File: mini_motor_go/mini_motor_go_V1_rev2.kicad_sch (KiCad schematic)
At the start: 30 parts, among them J10 Conn_01x02_Pin, J11 USB4520-03-0-A_REVA, J12 BM05B-SRSS-TB_LF__SN_, J13 BM05B-SRSS-TB_LF__SN_, J3 I2C_STANDARDQWIIC, J5 I2C_STANDARDQWIIC, J9 Conn_01x09_Pin, U1 ESP32-S3-WROOM-1

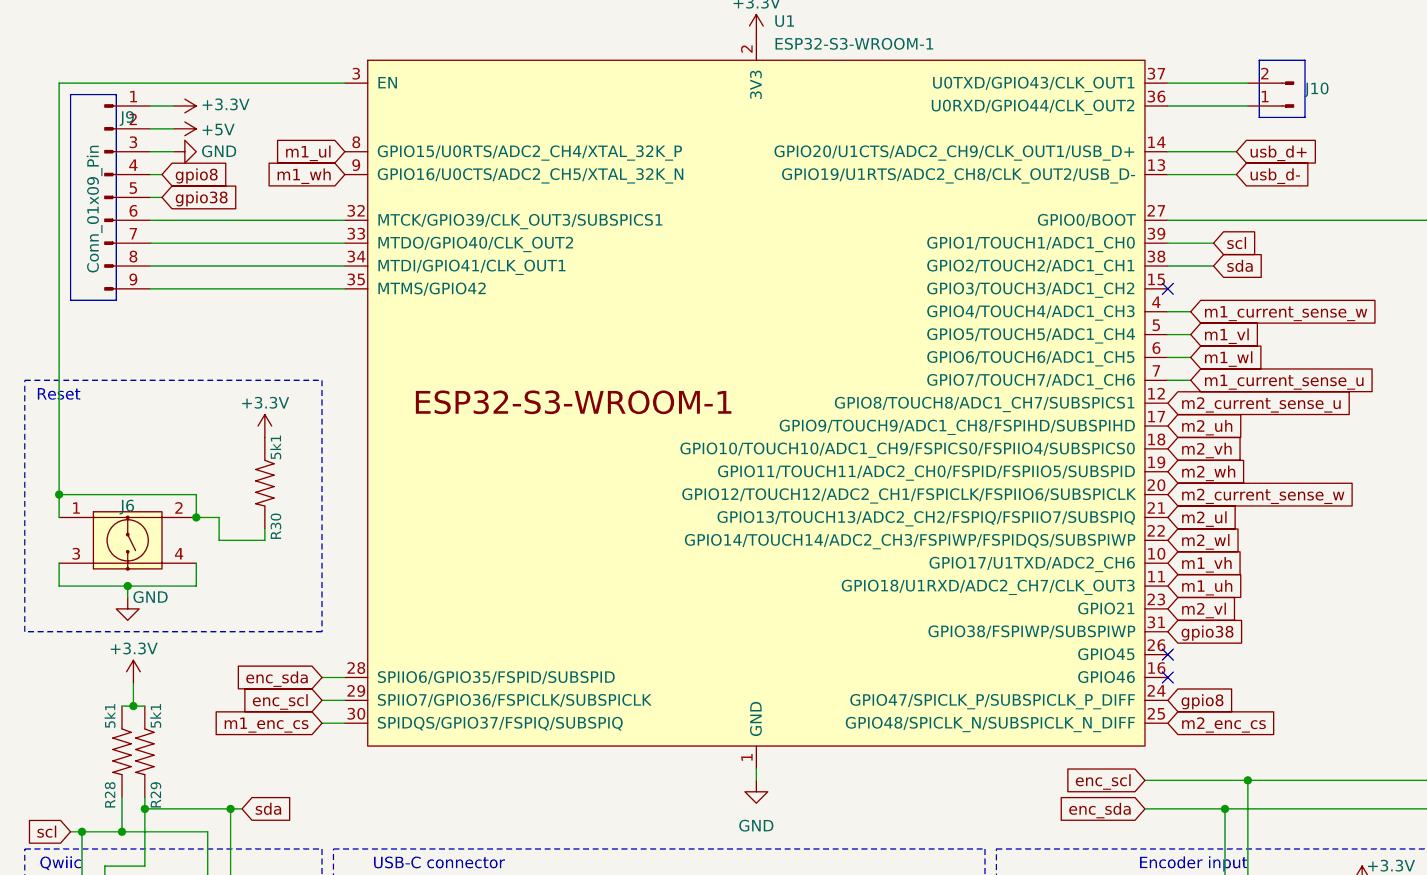
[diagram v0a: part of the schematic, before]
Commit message: slight update to part selection table
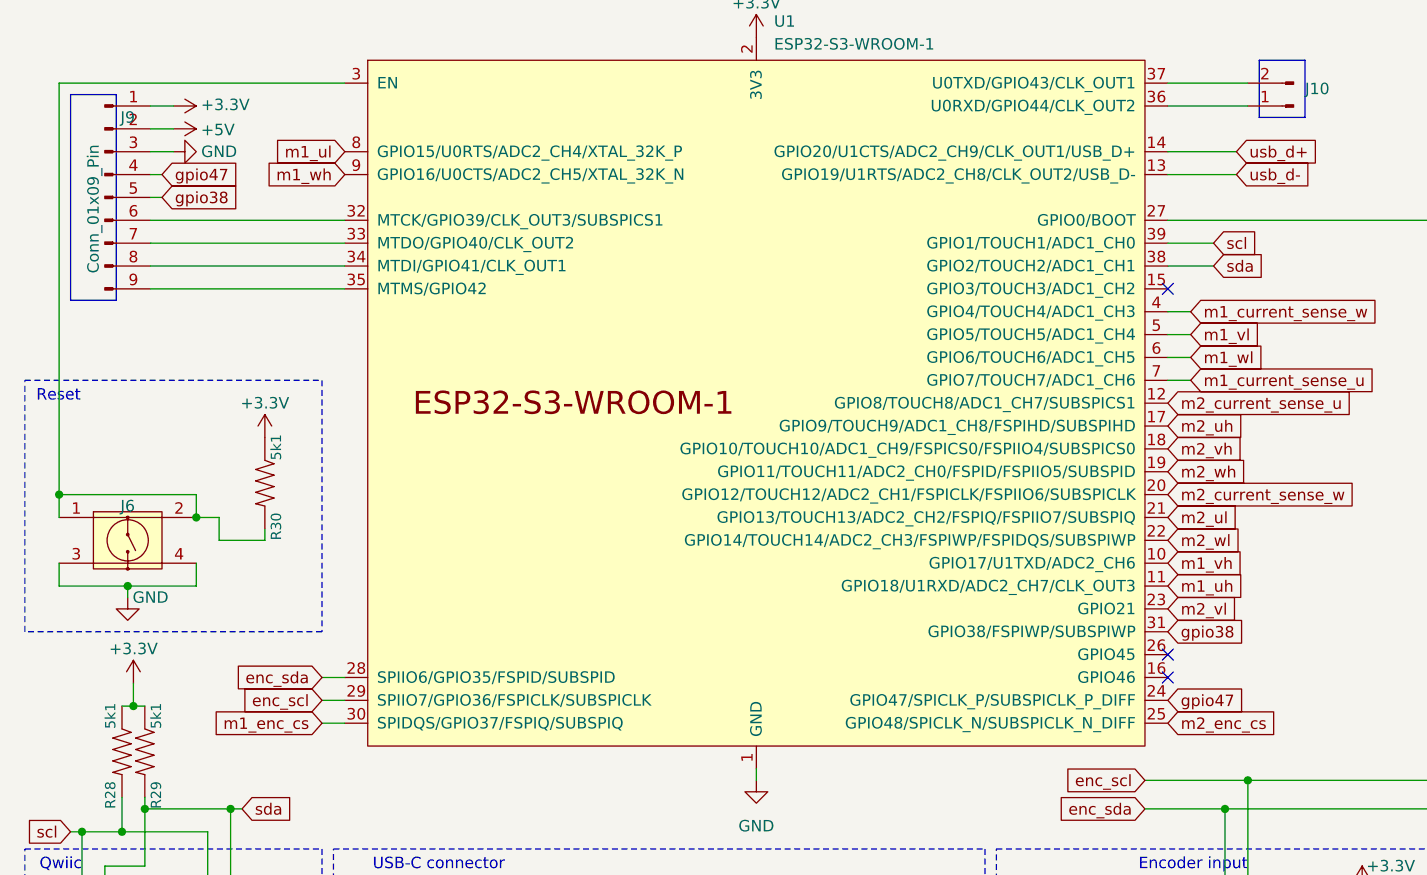
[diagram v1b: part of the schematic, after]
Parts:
- D1, D2, D3: footprint LED_SMD:LED_0805_2012Metric_Pad1.15x1.40mm_HandSolder -> LED_SMD:LED_0805_2012Metric
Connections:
- net gpio8: no longer J9.4 (Pin_4), U1.24 (GPIO47/SPICLK_P/SUBSPICLK_P_DIFF)
- new net gpio47: J9.4 (Pin_4), U1.24 (GPIO47/SPICLK_P/SUBSPICLK_P_DIFF)
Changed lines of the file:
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@@
     )
   )
-  (global_label "gpio8" (shape input) (at 29.21 40.64 0) (fields_autoplaced)
-    (effects (font (size 1.27 1.27)) (justify left))
-    (property "Intersheetrefs" "${INTERSHEET_REFS}" (at 37.3771 40.64 0)
+  (global_label "gpio47" (shape input) (at 29.21 40.64 0) (fields_autoplaced)
+    (effects (font (size 1.27 1.27)) (justify left))
+    (property "Intersheetrefs" "${INTERSHEET_REFS}" (at 38.5866 40.64 0)
       (effects (font (size 1.27 1.27)) (justify left) hide)
     )
@@
     )
   )
-  (global_label "gpio8" (shape input) (at 140.97 99.06 0) (fields_autoplaced)
-    (effects (font (size 1.27 1.27)) (justify left))
-    (property "Intersheetrefs" "${INTERSHEET_REFS}" (at 149.1371 99.06 0)
+  (global_label "gpio47" (shape input) (at 140.97 99.06 0) (fields_autoplaced)
+    (effects (font (size 1.27 1.27)) (justify left))
+    (property "Intersheetrefs" "${INTERSHEET_REFS}" (at 150.3466 99.06 0)
       (effects (font (size 1.27 1.27)) (justify left) hide)
     )
@@
       (effects (font (size 1.27 1.27)) (justify right))
     )
-    (property "Footprint" "LED_SMD:LED_0805_2012Metric_Pad1.15x1.40mm_HandSolder" (at 38.1 176.53 0)
+    (property "Footprint" "LED_SMD:LED_0805_2012Metric" (at 38.1 176.53 0)
       (effects (font (size 1.27 1.27)) hide)
     )
@@
       (effects (font (size 1.27 1.27)) (justify right))
     )
-    (property "Footprint" "LED_SMD:LED_0805_2012Metric_Pad1.15x1.40mm_HandSolder" (at 19.05 176.53 0)
+    (property "Footprint" "LED_SMD:LED_0805_2012Metric" (at 19.05 176.53 0)
       (effects (font (size 1.27 1.27)) hide)
     )
@@
       (effects (font (size 1.27 1.27)) (justify right))
     )
-    (property "Footprint" "LED_SMD:LED_0805_2012Metric_Pad1.15x1.40mm_HandSolder" (at 27.94 176.53 0)
-      (effects (font (size 1.27 1.27)) hide)
-    )
+    (property "Footprint" "LED_SMD:LED_0805_2012Metric" (at 27.94 176.53 0)
+      (effects (font (size 1.27 1.27)) hide)
+    )
